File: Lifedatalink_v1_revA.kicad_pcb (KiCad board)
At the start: 4 copper layers, 62.4 x 72.4 mm, 93 parts, among them J1 DX07S024XJ1R1100, J10 503480-0400, J11 5034801400, J12 5034801400, J13 503480-0600, J14 503480-0600, J15 503480-0600, J16 503480-0600, J17 503480-0600, J18 ECG_RIGHT_LEG, J19 MOUNTING_HOLE_MAIN, J2 SM02B-SRSS-TB(LF)(SN), J20 MOUNTING_HOLE_ECG, J3 503480-0600, J4 Conn_01x06, J5 503480-0600, J6 ECG_LEFT_ARM, J7 ECG_RIGHT_ARM, J8 503480-0600, J9 503480-0400, P6 HORIZON MEDICAL LOGO, Q1 CSD23280F3, SW1 SW_Push, U1 BL654, U2 LP5907MFX-3_3_NOPB, U3 ADS1292RIRSMT, U4 MCP73831T-2ACI/OT, U5 TMP117NAIYBGR, U6 MAX30102, U7 LP5907MFX-1.8/NOPB, U8 IIS2DLPCTR, U9 PCA9306DQER, Y1 Crystal

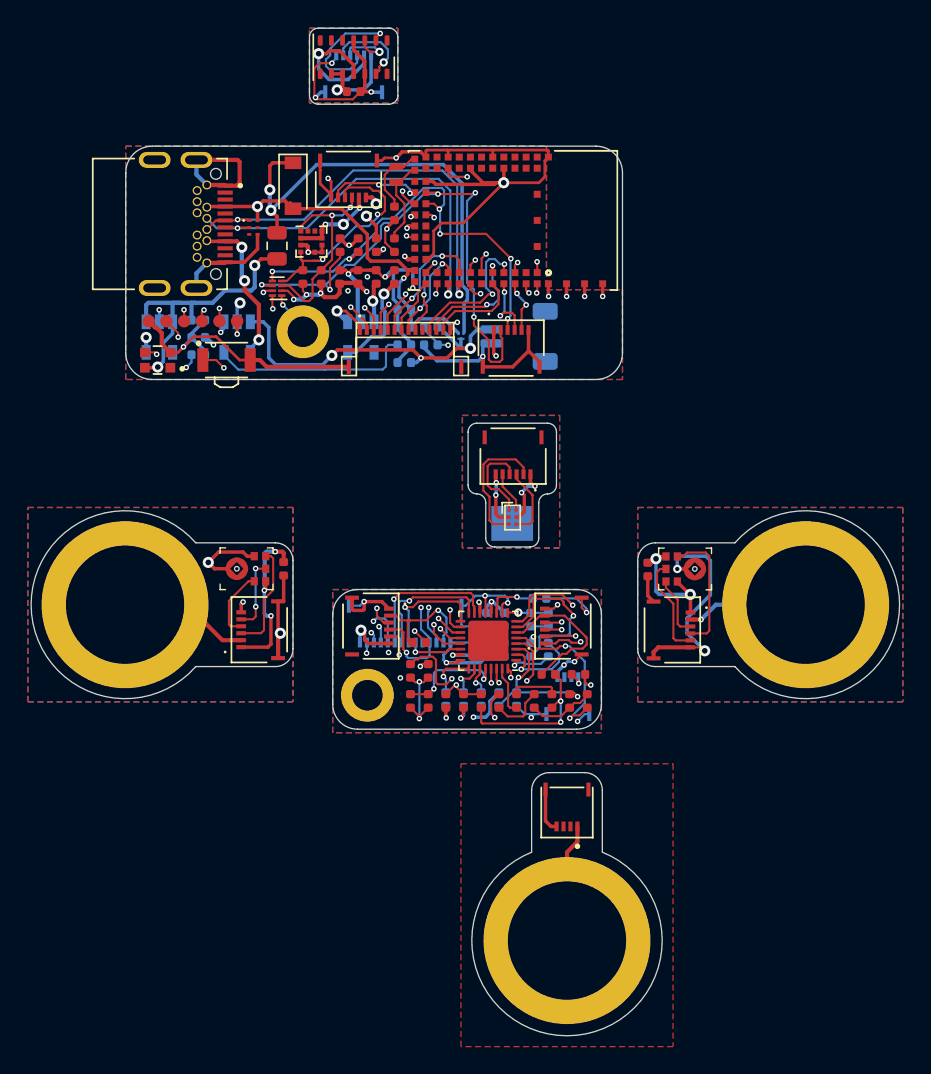
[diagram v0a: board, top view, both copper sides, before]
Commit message: Update schematic components
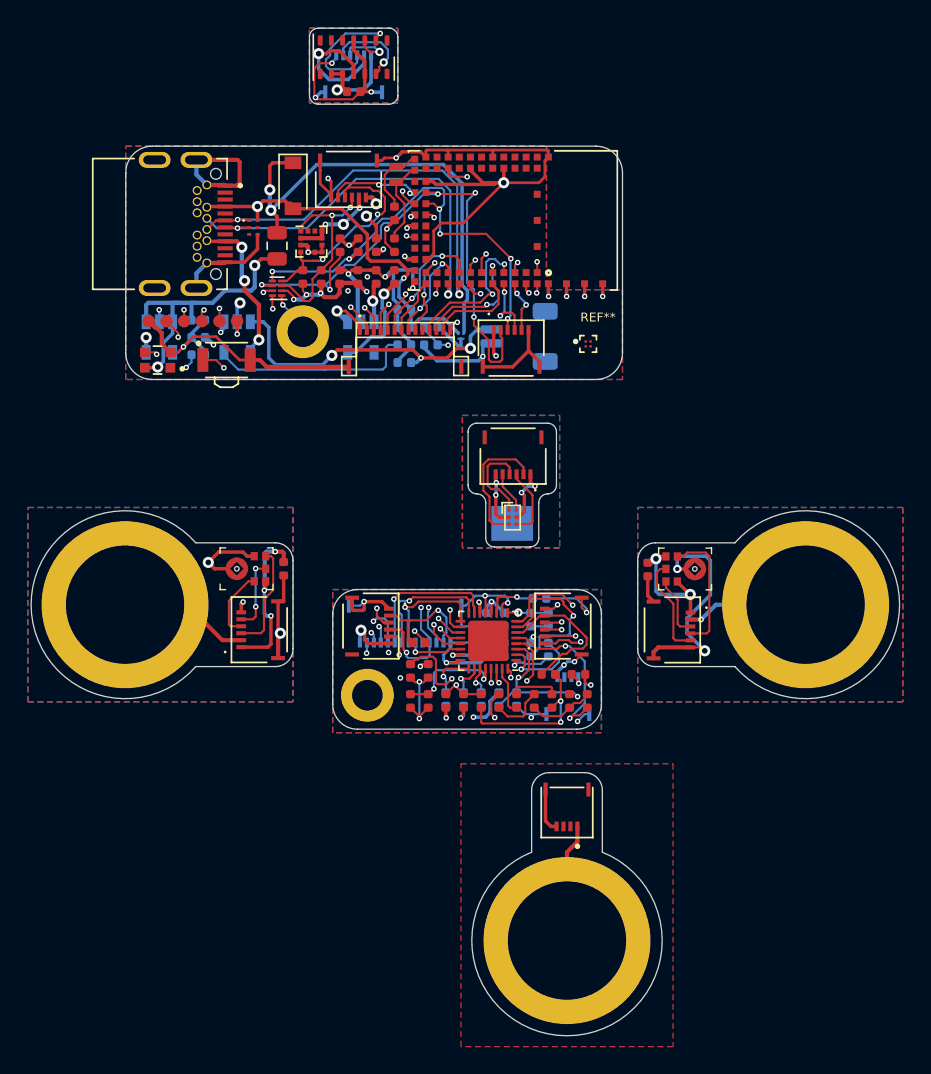
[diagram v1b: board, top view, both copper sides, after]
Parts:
- added REF**: BGA4N35P2X2_64X64X33, Footprints:BGA4N35P2X2_64X64X33, F.Cu at (101.1, 94.8)
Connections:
- net /~ADS_DRDY renamed /~{ADS_DRDY}
- net /~ADS_DRDY_EXT renamed /~{ADS_DRDY_EXT}
- net /~ADS_PWDN_RESET renamed /~{ADS_PWDN_RESET}
- net /~ADS_PWDN_RESET_EXT renamed /~{ADS_PWDN_RESET_EXT}
- net /~ADS_SPI_CS renamed /~{ADS_SPI_CS}
- net /~ADS_SPI_CS_EXT renamed /~{ADS_SPI_CS_EXT}
- net /~MAX_INT renamed /~{MAX_INT}
- net /~MAX_INT_EXT renamed /~{MAX_INT_EXT}
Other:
- net class Default removed
- net class Power removed

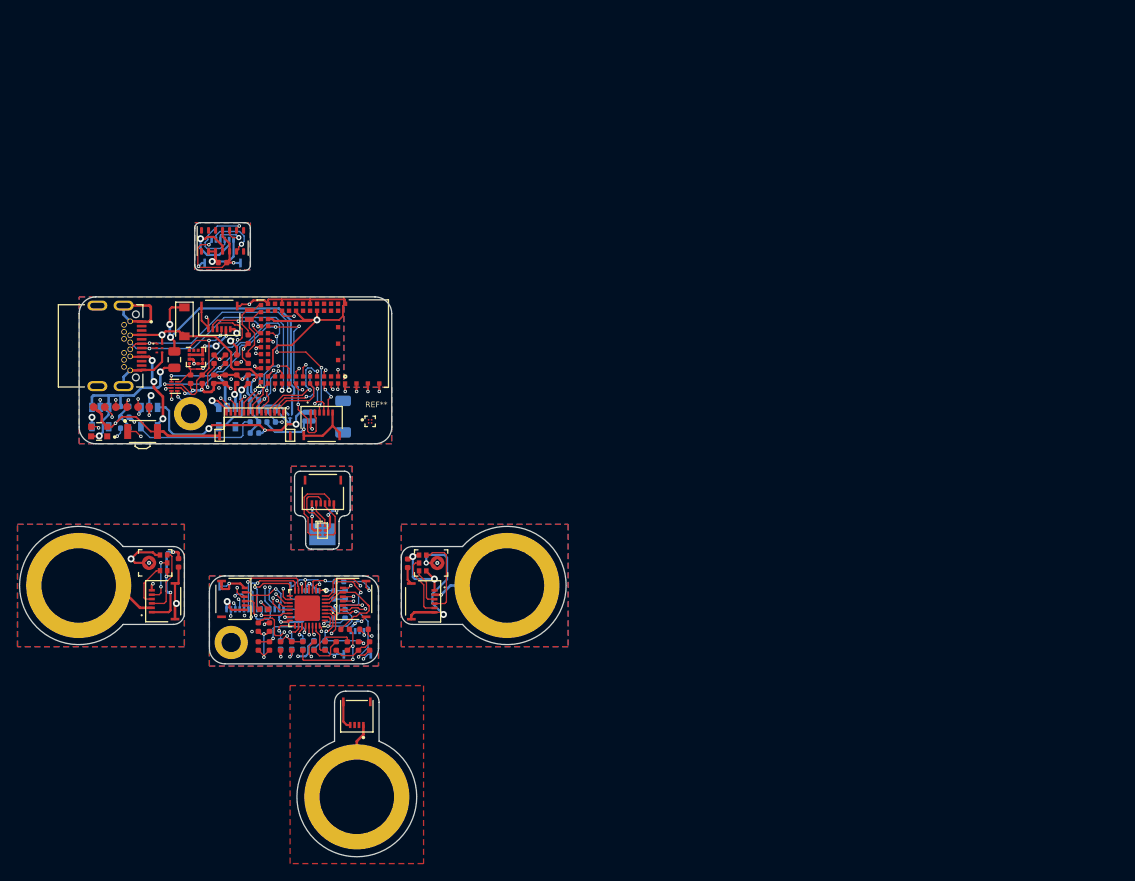
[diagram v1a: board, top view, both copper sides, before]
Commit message: Update PCB form factor and place components
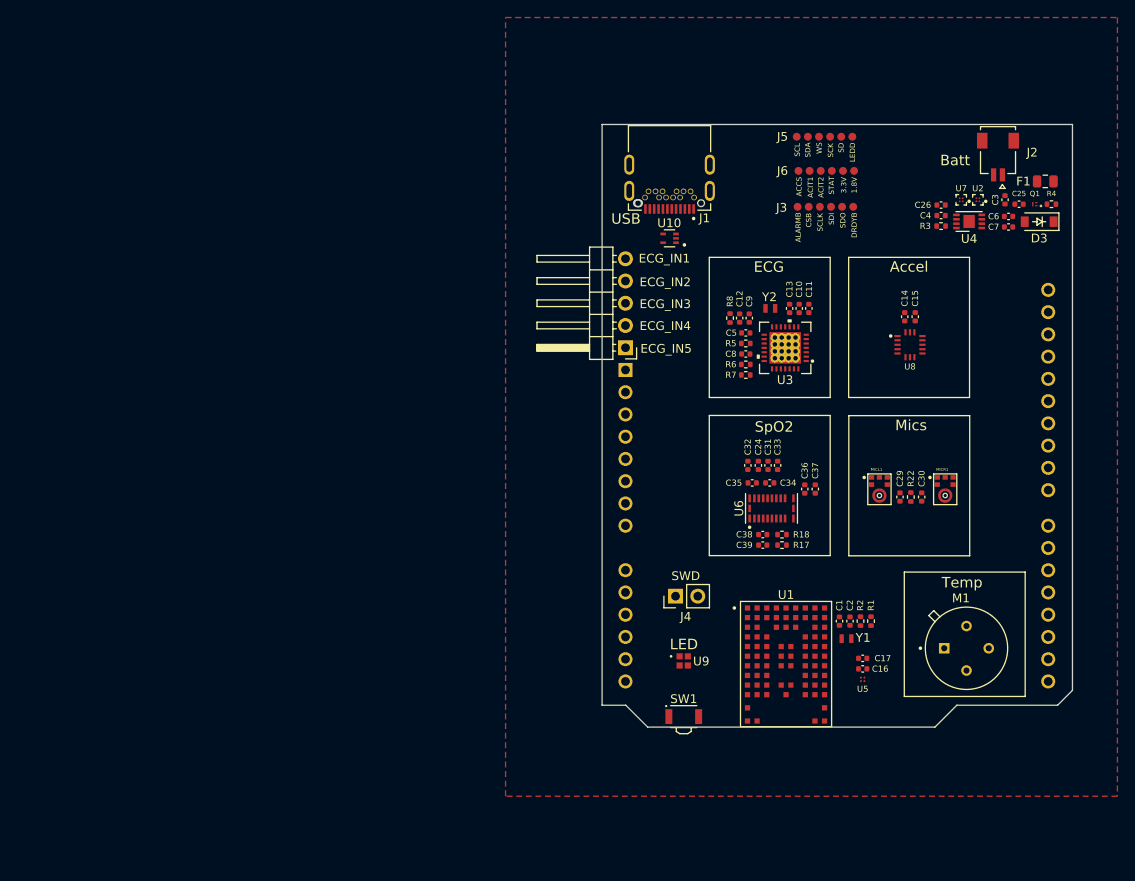
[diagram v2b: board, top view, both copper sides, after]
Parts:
- removed C18, C20: 2.2nF, Capacitor_SMD:C_0402_1005Metric
- removed C19, C23, C27: 100nF, Capacitor_SMD:C_0402_1005Metric
- removed C21: 47pF, Capacitor_SMD:C_0402_1005Metric
- removed C22, C28: 10uF, Capacitor_SMD:C_0402_1005Metric
- removed D1: TPD4S012DRYR, SnapEda:SON50P100X145X60-6N
- removed D2: WS2812B, APA-102-2020-256-8:LED_WS2812-2020
- removed J10, J9: 503480-0400, 503480-0400:MOLEX_503480-0400
- removed J11, J12: 5034801400, MOLEX_503480-0600:5034801400
- removed J13, J14, J15, J16, J17, J8: 503480-0600, MOLEX_503480-0600:MOLEX_503480-0600
- removed J18: ECG_RIGHT_LEG, MOLEX_503480-0600:ECG_SNAP
- removed J19: MOUNTING_HOLE_MAIN, MountingHole:MountingHole_2.2mm_M2_DIN965_Pad
- removed J20: MOUNTING_HOLE_ECG, MountingHole:MountingHole_2.2mm_M2_DIN965_Pad
- removed MIC1, MIC2: ICS-43434, digikey-footprints:SPH0645LM4H-B
- removed P6: HORIZON MEDICAL LOGO, horizon_logo_silk:horizon_logo_silk_small
- removed R10, R9: 10M, Resistor_SMD:R_0402_1005Metric
- removed R11: 1M, Resistor_SMD:R_0402_1005Metric
- removed R12, R14: 100K, Resistor_SMD:R_0402_1005Metric
- removed R13: 0R, Resistor_SMD:R_0402_1005Metric
- removed R15, R16: 45.3K, Resistor_SMD:R_0402_1005Metric
- removed R19, R20, R21: 4.7K, Resistor_SMD:R_0402_1005Metric
- removed REF**: BGA4N35P2X2_64X64X33, Footprints:BGA4N35P2X2_64X64X33
- removed REF**: TEMP_SENSOR_PAD, Pads_1.27mm:TEMP_SENSOR_PAD
- added A1: Arduino_UNO_R3, Module:Arduino_UNO_R3, B.Cu at (130.2, 88.9)
- added C32: 0.1uF, Capacitor_SMD:C_0402_1005Metric, F.Cu at (144.2, 99.8)
- added C33: 4.7uF, Capacitor_SMD:C_0402_1005Metric, F.Cu at (147.6, 99.8)
- added C34: 1uF, Capacitor_SMD:C_0402_1005Metric, F.Cu at (146.7, 101.8)
- added C35: 1uF, Capacitor_SMD:C_0402_1005Metric, F.Cu at (144.7, 101.8)
- added C36: 10uF, Capacitor_SMD:C_0402_1005Metric, F.Cu at (150.7, 102.5)
- added C37: 1uF, Capacitor_SMD:C_0402_1005Metric, F.Cu at (151.9, 102.5)
- added C38: 10pF, Capacitor_SMD:C_0402_1005Metric, F.Cu at (145.9, 107.7)
- added C39: 10pF, Capacitor_SMD:C_0402_1005Metric, F.Cu at (145.9, 108.9)
- added M1: MLX90614ESF-AAA-000-TU, Footprints:TO254P940H1340-4, F.Cu at (169.2, 120.7)
- added MICL1: ICS-43434, Footprints:MIC_ICS-43434, F.Cu at (159.2, 102.6)
- added MICR1: ICS-43434, Footprints:MIC_ICS-43434, F.Cu at (166.7, 102.6)
- added U10: TPD2E001IDRLRQ1, Footprints:SOT50P160X60-5N, F.Cu at (135.3, 73.9)
- added Y2: Crystal, ABS05-32.768KHZ-T:ABS05-32.768KHZ-T, F.Cu at (146.2, 81.9)
- C10: value 100nF -> 22pF; moved to F.Cu
- C11, C12: value 1uF -> 0.1uF; moved to F.Cu
- C13, C14: value 47nF -> 0.1uF; moved to F.Cu
- C15: value 2.2nF -> 10uF
- C16: value 2.2nF -> 0.1uF
- C17: value 100nF -> 0.1uF
- C24: value 1uF -> 0.1uF
- C3, C4, C6, C7, Q1, R1, R2, R4: moved to F.Cu
- C31: value 100pF -> 4.7uF; moved to F.Cu
- C5: value 10uF -> 1.5nF; moved to F.Cu
- C8: value 100nF -> 0.1uF; moved to F.Cu
- C9: value 10uF -> 22pF; moved to F.Cu
- D3: value MBR0540T1G -> SS0540_R1_00001
- J2: value SM02B-SRSS-TB(LF)(SN) -> 5015680207; footprint Connector_JST:JST_SH_SM02B-SRSS-TB_1x02-1MP_P1.00mm_Horizontal -> Footprints:MOLEX_5015680207; moved to F.Cu
- J3, J5: value 503480-0600 -> Conn_01x06; footprint MOLEX_503480-0600:MOLEX_503480-0600 -> Pads_1.27mm:1.27mm_pads_01x06
- J4: value Conn_01x06 -> Conn_01x02; footprint Pads_1.27mm:1.27mm_pads_01x06 -> Connector_PinHeader_2.54mm:PinHeader_1x02_P2.54mm_Vertical
- J6: value ECG_LEFT_ARM -> Conn_01x06; footprint MOLEX_503480-0600:ECG_SNAP -> Pads_1.27mm:1.27mm_pads_01x06
- J7: value ECG_RIGHT_ARM -> ECG_IN; footprint MOLEX_503480-0600:ECG_SNAP -> Connector_PinHeader_2.54mm:PinHeader_1x05_P2.54mm_Horizontal
- R17: value 200K -> 50K
- R18: value 4.7K -> 50K
- R3: value 10K -> 2K; moved to F.Cu
- R5: value 10M -> 100K
- R6: value 10M -> 1M
- R7, R8: value 40.2K -> 1M
- U1: value BL654 -> NORA-B106-00B; footprint XCVR_451-00001:XCVR_451-00001 -> Footprints:XCVR_NORA-B106-00B
- U2: value LP5907MFX-3_3_NOPB -> TCR3UG33A,LF; footprint Package_TO_SOT_SMD:SOT-23-5 -> Footprints:BGA4N35P2X2_64X64X33; moved to F.Cu
- U3: value ADS1292RIRSMT -> ADS1293CISQE/NOPB; footprint Package_DFN_QFN:QFN-32-1EP_4x4mm_P0.4mm_EP2.9x2.9mm -> Footprints:ADS1293CISQE
- U4: value MCP73831T-2ACI/OT -> MCP73831T-3ACI/MC; footprint Package_TO_SOT_SMD:SOT-23-5 -> Package_DFN_QFN:DFN-8-1EP_3x2mm_P0.5mm_EP1.3x1.5mm; moved to F.Cu
- U5: value TMP117NAIYBGR -> LMT70AYFQT; footprint Package_BGA:Texas_DSBGA-6_0.9x1.4mm_Layout2x3_P0.5mm -> Footprints:BGA4C40P2X2_88X88X68
- U6: value MAX30102 -> MAX86150EFF+T; footprint OptoDevice:Maxim_OLGA-14_3.3x5.6mm_P0.8mm -> Footprints:XDCR_MAX86150EFF+
- U7: value LP5907MFX-1.8/NOPB -> TCR3UG18A,LF; footprint Package_TO_SOT_SMD:SOT-23-5 -> Footprints:BGA4N35P2X2_64X64X33; moved to F.Cu
- U8: value IIS2DLPCTR -> LIS331DLHTR; footprint Package_LGA:LGA-12_2x2mm_P0.5mm -> Footprints:LGA16R50P3X5_300X300X100
- U9: value PCA9306DQER -> LTST-E263CEGBK; footprint Package_SON:X2SON-8_1.4x1mm_P0.35mm -> Footprints:LTST-E263CEGBK
- moved C3 103.2 mm to (173.6, 69.5), turned to -90 degrees
- moved U2 103.2 mm to (170.5, 69.5), turned to 180 degrees
- moved F1 101.5 mm to (178.2, 67.4), turned to 180 degrees
- moved D3 98.3 mm to (177.5, 72.0), turned to 180 degrees
- moved U4 96.2 mm to (169.5, 72.0), turned to 180 degrees
- moved C4 96.0 mm to (166.3, 71.3)
- moved R4 94.0 mm to (178.9, 70.0), turned to 180 degrees
- moved C25 91.5 mm to (175.2, 70.0), turned to 0 degrees
- moved C7 89.2 mm to (174.0, 72.6), turned to 180 degrees
- moved C6 88.6 mm to (174.0, 71.4), turned to 180 degrees
- moved Q1 88.4 mm to (177.0, 70.0), turned to 180 degrees
- moved U7 87.4 mm to (168.6, 69.5), turned to 180 degrees
- moved C29 82.7 mm to (161.6, 103.4), turned to -90 degrees
- moved J2 82.4 mm to (172.8, 64.1), turned to 180 degrees
- moved C26 81.6 mm to (166.3, 70.1), turned to 0 degrees
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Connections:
- net /ECG_RIGHT_ARM renamed Net-(J7-Pin_1)
- C1 pad 1: Net-(C1-Pad1) -> Net-(U1-P0.00/XL1)
- C10 pad 1: GND -> Net-(U3-XTAL1)
- C10 pad 2: Net-(C10-Pad2) -> +3V3
- C11 pad 2: Net-(C11-Pad2) -> +3V3
- C12 pad 2: Net-(C12-Pad2) -> +3V3
- C13 pad 1: Net-(C13-Pad1) -> GND
- C13 pad 2: Net-(C13-Pad2) -> Net-(U3-CVREF)
- C14 pad 1: Net-(C14-Pad1) -> GND
- C14 pad 2: Net-(C14-Pad2) -> +3V3
- C15 pad 1: Net-(C15-Pad1) -> GND
- C15 pad 2: Net-(C15-Pad2) -> +3V3
- C16 pad 1: Net-(C16-Pad1) -> GND
- C16 pad 2: Net-(C15-Pad1) -> +3V3
- C17 pad 1: Net-(C15-Pad1) -> GND
- C17 pad 2: /ECG_LEFT_ARM -> +3V3
- C2 pad 1: Net-(C2-Pad1) -> Net-(U1-P0.01/XL2)
- C24 pad 2: +3V3 -> +1V8
- C31 pad 2: Net-(C31-Pad2) -> +1V8
- C5 pad 1: GND -> Net-(U3-RLDOUT)
- C5 pad 2: +3V3 -> Net-(U3-RLDINV)
- C8 pad 1: GND -> Net-(U3-RLDIN)
- C8 pad 2: +3V3 -> GND
- C9 pad 1: GND -> Net-(U3-XTAL2)
- C9 pad 2: Net-(C10-Pad2) -> +3V3
- J1 pad A10: Net-(J1-PadA10) -> unconnected-(J1-SSRXN2)
- J1 pad A11: Net-(J1-PadA11) -> unconnected-(J1-SSRXP2)
- J1 pad A2: Net-(J1-PadA2) -> unconnected-(J1-SSTXP1)
- J1 pad A3: Net-(J1-PadA3) -> unconnected-(J1-SSTXN1)
- J1 pad A5: Net-(J1-PadA5) -> unconnected-(J1-CC1)
- J1 pad A6: /BL654_USB_DP -> /NORA_USB_DP
- J1 pad A7: /BL654_USB_DN -> /NORA_USB_DM
- J1 pad A8: Net-(J1-PadA8) -> unconnected-(J1-SUB1)
- J1 pad B10: Net-(J1-PadB10) -> unconnected-(J1-SSRXN1)
- J1 pad B11: Net-(J1-PadB11) -> unconnected-(J1-SSRXP1)
- J1 pad B2: Net-(J1-PadB2) -> unconnected-(J1-SSTXP2)
- J1 pad B3: Net-(J1-PadB3) -> unconnected-(J1-SSTXN2)
- J1 pad B5: Net-(J1-PadB5) -> unconnected-(J1-CC2)
- J1 pad B6: /BL654_USB_DP -> /NORA_USB_DP
- J1 pad B7: /BL654_USB_DN -> /NORA_USB_DM
- J1 pad B8: Net-(J1-PadB8) -> unconnected-(J1-SUB2)
- J3 pad 1: GND -> /ADS_ALARMB
- J3 pad 2: /BL654_I2S_SD_EXT -> /ADS_CSB
- J3 pad 3: /BL654_I2S_SCK_EXT -> /ADS_SCLK
- J3 pad 4: /BL654_I2S_WS_EXT -> /ADS_SDI
- J3 pad 5: /ECG_LEFT_ARM -> /ADS_SDO
- J3 pad 6: +3V3 -> /ADS_DRDYB
- J4 pad 1: +3V3 -> /NORA_SWDCLK
- J4 pad 2: /BL654_SWDCLK -> /NORA_SWDIO
- J5 pad 1: +3V3 -> /NORA_I2C_SCL
- J5 pad 2: /ECG_LEFT_ARM -> /NORA_I2C_SDA
- J5 pad 3: /BL654_I2S_WS_EXT -> /NORA_I2S_WS
- J5 pad 4: /BL654_I2S_SCK_EXT -> /NORA_I2S_SCK
- J5 pad 5: /BL654_I2S_SD_EXT -> /NORA_I2S_SD
- J5 pad 6: GND -> /LED_DATA
- J6 pad 1: /ECG_LEFT_ARM -> /ACCEL_CS
- R1 pad 1: /VDIV -> /BAT_VDIV
- R17 pad 1: +3V3 -> ECG_N
- R17 pad 2: Net-(C31-Pad2) -> Net-(U6-ECG_N)
- R18 pad 1: +1V8 -> ECG_N
- R18 pad 2: /BL654_I2C_SDA_LV -> Net-(U6-ECG_P)
- R2 pad 2: /VDIV -> /BAT_VDIV
- R22 pad 1: /BL654_I2S_SD_EXT -> /NORA_I2S_SD_EXT
- R5 pad 1: Net-(C15-Pad2) -> Net-(U3-CMOUT)
- R5 pad 2: +3V3 -> Net-(U3-RLDINV)
- R6 pad 1: Net-(C15-Pad2) -> Net-(U3-RLDOUT)
- R6 pad 2: GND -> Net-(U3-RLDINV)
- R7 pad 1: Net-(R7-Pad1) -> Net-(U3-SYNCB)
- R7 pad 2: Net-(C16-Pad1) -> +3V3
- R8 pad 1: Net-(R8-Pad1) -> Net-(U3-RSTB)
- R8 pad 2: Net-(C18-Pad1) -> +3V3
- SW1 pad 1: Net-(SW1-Pad1) -> Net-(U1-P1.12)
- U3 pad 1: Net-(C13-Pad2) -> Net-(J7-Pin_5)
- U3 pad 10: GND -> Net-(U3-RLDINV)
- U3 pad 11: Net-(C11-Pad2) -> Net-(U3-RLDIN)
- U3 pad 12: +3V3 -> Net-(U3-RLDIN)
- U3 pad 13: GND -> Net-(U3-SYNCB)
- U3 pad 14: +3V3 -> GND
- U3 pad 15: /~{ADS_PWDN_RESET_EXT} -> /ADS_ALARMB
- U3 pad 16: /ADS_START_EXT -> /ADS_CSB
- U3 pad 17: /ADS_CLK_EXT -> /ADS_SCLK
- U3 pad 18: /~{ADS_SPI_CS_EXT} -> /ADS_SDI
- U3 pad 19: /ADS_SPI_MOSI_EXT -> /ADS_SDO
- U3 pad 2: Net-(C13-Pad1) -> Net-(J7-Pin_4)
- U3 pad 20: /ADS_SPI_SCLK_EXT -> /ADS_DRDYB
- U3 pad 21: /ADS_SPI_MISO_EXT -> /ADS_CLK
- U3 pad 22: /~{ADS_DRDY_EXT} -> +3V3
- U3 pad 23: +3V3 -> Net-(U3-XTAL1)
- U3 pad 24: GND -> Net-(U3-XTAL2)
- U3 pad 25: Net-(R16-Pad1) -> Net-(U3-RSTB)
- U3 pad 26: Net-(R15-Pad1) -> Net-(U3-CVREF)
- U3 pad 27: Net-(C12-Pad2) -> GND
- U3 pad 28: /RLDINV -> +3V3
- U3 pad 29: /RLDIN -> unconnected-(U3-EPAD)
- U3 pad 3: Net-(C20-Pad2) -> Net-(J7-Pin_3)
- U3 pad 4: Net-(C15-Pad2) -> Net-(J7-Pin_2)
- U3 pad 6: /ECG_LEFT_ARM -> unconnected-(U3-IN6)
- U3 pad 7: Net-(C14-Pad2) -> unconnected-(U3-WCT)
- U3 pad 8: Net-(C14-Pad1) -> Net-(U3-CMOUT)
- U3 pad 9: Net-(C10-Pad2) -> Net-(U3-RLDOUT)
- U5 pad A1: /BL654_I2C_SDA_HV_EXT -> GND
- U5 pad A2: /BL654_I2C_SCL_HV_EXT -> +3V3
- U5 pad B1: +3V3 -> /TEMP_ADC_OUT
- U5 pad B2: GND -> +3V3
- U6 pad 1: Net-(U6-Pad1) -> unconnected-(U6-N.C.-1)
- U6 pad 10: +3V3 -> unconnected-(U6-N.C.)
- U6 pad 11: +1V8 -> unconnected-(U6-N.C.-6)
- U6 pad 12: GND -> unconnected-(U6-N.C.-7)
- U6 pad 13: /~{MAX_INT_EXT} -> +1V8
- U6 pad 14: Net-(U6-Pad14) -> +1V8
- U6 pad 2: /BL654_I2C_SCL_LV_EXT -> unconnected-(U6-N.C.-2)
- U6 pad 3: /BL654_I2C_SDA_LV_EXT -> unconnected-(U6-N.C.-3)
- U6 pad 4: GND -> Net-(U6-ECG_N)
- U6 pad 5: Net-(U6-Pad5) -> Net-(U6-ECG_P)
- U6 pad 6: Net-(U6-Pad6) -> unconnected-(U6-N.C.-4)
- U6 pad 7: Net-(U6-Pad7) -> /~{MAX_INT}
- U6 pad 8: Net-(U6-Pad8) -> /NORA_I2C_SDA
- U6 pad 9: +3V3 -> /NORA_I2C_SCL
- U8 pad 1: /BL654_I2C_SCL_LV -> +3V3
- U8 pad 10: +1V8 -> GND
- U8 pad 11: /ACCEL_INT2 -> /ACCEL_INT1
- U8 pad 12: /ACCEL_INT1 -> GND
- U8 pad 2: +1V8 -> unconnected-(U8-NC_2)
- U8 pad 3: GND -> unconnected-(U8-NC)
- U8 pad 4: /BL654_I2C_SDA_LV -> /NORA_I2C_SCL
- U8 pad 6: GND -> /NORA_I2C_SDA
- U8 pad 8: GND -> /ACCEL_CS
- U8 pad 9: +1V8 -> /ACCEL_INT2
- U9 pad 1: GND -> /VIN
- U9 pad 2: +1V8 -> /LED_DATA
- U9 pad 3: /BL654_I2C_SCL_LV -> unconnected-(U9-DOUT)
- U9 pad 4: /BL654_I2C_SDA_LV -> GND
- Y1 pad 1: Net-(C1-Pad1) -> Net-(U1-P0.00/XL1)
- Y1 pad 2: Net-(C2-Pad1) -> Net-(U1-P0.01/XL2)
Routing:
- net GND: track 308.2 -> 0.00 mm, vias 42 -> 0
- net +3V3: track 144.0 -> 0.00 mm, vias 28 -> 0
- net +5V: track 43.6 -> 0.00 mm, vias 5 -> 0
- net /BL654_I2C_SCL_HV: track 40.1 -> 0.00 mm, vias 5 -> 0
- net +1V8: track 39.8 -> 0.00 mm, vias 9 -> 0
- net /WS2812_DATA: track 38.0 -> 0.00 mm, vias 2 -> 0
- net Net-(J7-Pin_1): track 36.1 -> 0.00 mm, vias 3 -> 0
- net /BL654_I2S_SD_EXT: track 35.5 -> 0.00 mm, vias 4 -> 0
- net /BL654_I2S_SCK_EXT: track 34.8 -> 0.00 mm, vias 3 -> 0
- net /VIN_FUSE: track 33.6 -> 0.00 mm, vias 2 -> 0
- net /BL654_I2S_WS_EXT: track 33.1 -> 0.00 mm, vias 3 -> 0
- net /BL654_I2C_SDA_HV: track 32.5 -> 0.00 mm, vias 6 -> 0
- net /BL654_SWDIO: track 31.7 -> 0.00 mm, vias 3 -> 0
- net Net-(SW1-Pad1): track 31.3 -> 0.00 mm, vias 2 -> 0
- net /BL654_SWDCLK: track 29.7 -> 0.00 mm, vias 3 -> 0
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- removed copper zone on In2.Cu, net +3V3
- removed copper zone on B.Cu, net GND
- removed copper zone on In1.Cu, net GND
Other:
- board size 62.4 x 72.4 mm -> 53.7 x 68.8 mm
- rule pad_to_mask_clearance: 0.051 -> 0
- board text added: "1.8V"
- board text added: "3.3V"
- board text added: "ACCS"
- board text added: "ACIT1"
- board text added: "ACIT2"
- board text added: "ALARMB"
- board text added: "Accel"
- board text added: "Batt"
- board text added: "CSB"
- board text added: "DRDYB"
- board text added: "ECG"
- board text added: "ECG_IN1"
- board text added: "ECG_IN2"
- board text added: "ECG_IN3"
- board text added: "ECG_IN4"
- board text added: "ECG_IN5"
- board text added: "LED"
- board text added: "LEDD"
- board text added: "Mics"
- board text added: "SCK"
- board text added: "SCL"
- board text added: "SCLK"
- board text added: "SD"
- board text added: "SDA"
- board text added: "SDI"
- board text added: "SDO"
- board text added: "STAT"
- board text added: "SWD"
- board text added: "SpO2"
- board text added: "Temp"
- board text added: "USB"
- board text added: "WS"
- board text removed: "Designed by HORIZON MEDICAL S.A.S. Cartagena - Colombia www.horizonmedical.co Model: HZLDL1A"

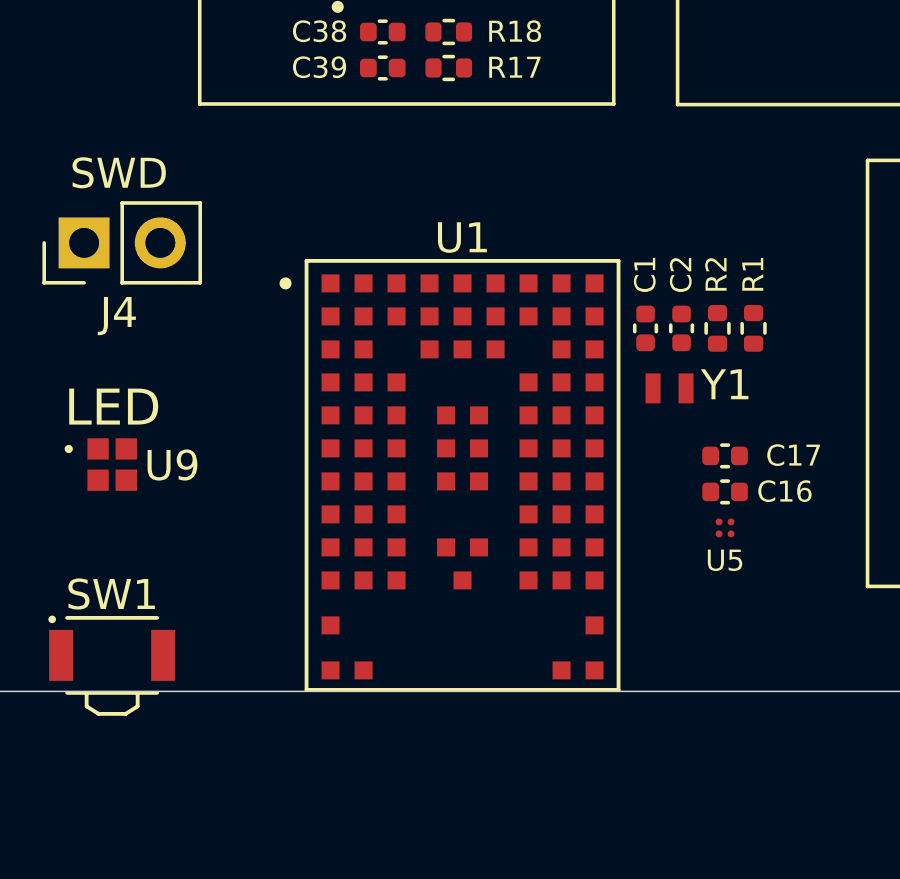
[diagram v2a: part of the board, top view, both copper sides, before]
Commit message: Replace the BLE module with a BL5340 (453-00053R)
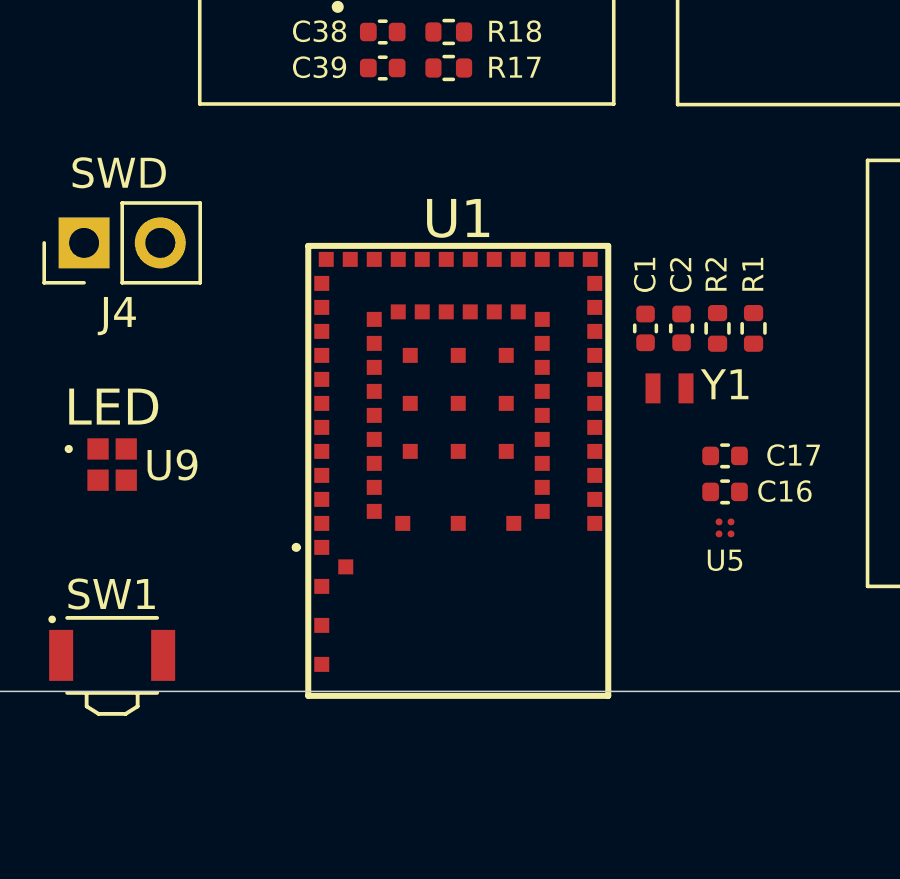
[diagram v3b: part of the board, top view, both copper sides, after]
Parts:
- U1: value NORA-B106-00B -> 453-00052R; footprint Footprints:XCVR_NORA-B106-00B -> Footprints:45300052R
- moved U1 0.76 mm to (148.4, 122.4), turned to 180 degrees
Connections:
- net /NORA_I2S_SD_EXT renamed /ISP_I2S_SD_EXT
- A1 pad 15: /NORA_UART_RX -> /ISP_UART_RX
- A1 pad 16: /NORA_UART_TX -> /ISP_UART_TX
- C1 pad 1: Net-(U1-P0.00/XL1) -> Net-(U1-P0.01_/_XL2)
- C2 pad 1: Net-(U1-P0.01/XL2) -> Net-(U1-P0.00_/_XL1)
- J1 pad A6: /NORA_USB_DP -> /ISP_USB_DP
- J1 pad A7: /NORA_USB_DM -> /ISP_USB_DM
- J1 pad B6: /NORA_USB_DP -> /ISP_USB_DP
- J1 pad B7: /NORA_USB_DM -> /ISP_USB_DM
- J4 pad 1: /NORA_SWDCLK -> /ISP_SWDCLK
- J4 pad 2: /NORA_SWDIO -> /ISP_SWDIO
- J5 pad 1: /NORA_I2C_SCL -> /ISP_I2C_SCL
- J5 pad 2: /NORA_I2C_SDA -> /ISP_I2C_SDA
- J5 pad 3: /NORA_I2S_WS -> /ISP_I2S_WS
- J5 pad 4: /NORA_I2S_SCK -> /ISP_I2S_SCK
- J5 pad 5: /NORA_I2S_SD -> /ISP_I2S_SD
- MICL1 pad 1: /NORA_I2S_WS_EXT -> /ISP_I2S_WS
- MICL1 pad 4: /NORA_I2S_SCK_EXT -> /ISP_I2S_SCK
- MICR1 pad 1: /NORA_I2S_WS_EXT -> /ISP_I2S_WS
- MICR1 pad 4: /NORA_I2S_SCK_EXT -> /ISP_I2S_SCK
- SW1 pad 1: Net-(U1-P1.12) -> Net-(U1-P0.29)
- U10 pad 3: /NORA_USB_DP -> /ISP_USB_DP
- U10 pad 5: /NORA_USB_DM -> /ISP_USB_DM
- U6 pad 8: /NORA_I2C_SDA -> /ISP_I2C_SDA
- U6 pad 9: /NORA_I2C_SCL -> /ISP_I2C_SCL
- U8 pad 4: /NORA_I2C_SCL -> /ISP_I2C_SCL
- U8 pad 6: /NORA_I2C_SDA -> /ISP_I2C_SDA
- Y1 pad 1: Net-(U1-P0.00/XL1) -> Net-(U1-P0.01_/_XL2)
- Y1 pad 2: Net-(U1-P0.01/XL2) -> Net-(U1-P0.00_/_XL1)
